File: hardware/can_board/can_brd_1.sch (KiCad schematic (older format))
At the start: 11 parts, among them P471 CONN_4, P472 CONN_2, U471 SN65HVD230

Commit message: making progress
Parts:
- added M470, M471: CONN_1, symbol CONN_1
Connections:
- no-connect marks 1 -> 3
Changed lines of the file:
@@
 Sheet 1 1
 Title ""
-Date "19 jan 2014"
+Date "26 jan 2014"
 Rev ""
 Comp ""
@@
 	2200 1550 2300 1550
 Wire Wire Line
-	4250 2150 3550 2150
-Wire Wire Line
-	4250 1550 3550 1550
+	4250 2150 4000 2150
+Wire Wire Line
+	4250 1550 4000 1550
 Text Label 5500 1750 0    60   ~ 0
 CANH
@@
 Wire Wire Line
 	5725 2625 5600 2625
-Text GLabel 3550 1550 0    60   Input ~ 0
-CAN_RX
-Text GLabel 3550 2150 0    60   Input ~ 0
-CAN_TX
+$Comp
+L CONN_1 M470
+U 1 1 52E4A990
+P 6600 1050
+F 0 "M470" H 6680 1050 40  0000 L CNN
+F 1 "CONN_1" H 6600 1105 30  0001 C CNN
+F 2 "" H 6600 1050 60  0000 C CNN
+F 3 "" H 6600 1050 60  0000 C CNN
+	1    6600 1050
+	1    0    0    -1
+$EndComp
+NoConn ~ 6450 1050
+$Comp
+L CONN_1 M471
+U 1 1 52E4A9A2
+P 6600 1200
+F 0 "M471" H 6680 1200 40  0000 L CNN
+F 1 "CONN_1" H 6600 1255 30  0001 C CNN
+F 2 "" H 6600 1200 60  0000 C CNN
+F 3 "" H 6600 1200 60  0000 C CNN
+	1    6600 1200
+	1    0    0    -1
+$EndComp
+NoConn ~ 6450 1200
 $EndSCHEMATC

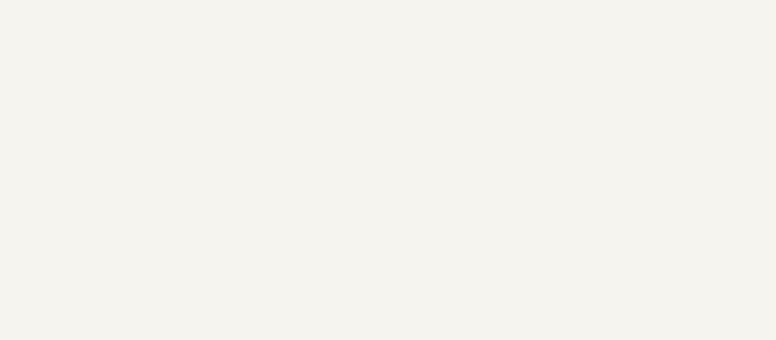
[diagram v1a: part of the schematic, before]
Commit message: 
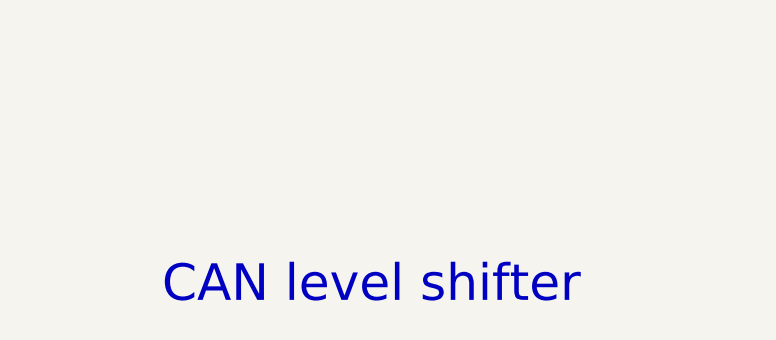
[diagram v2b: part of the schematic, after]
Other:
- note added: "CAN level shifter"
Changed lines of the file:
@@
 Sheet 1 1
 Title ""
-Date "26 jan 2014"
+Date "8 feb 2014"
 Rev ""
 Comp ""
@@
 $EndComp
 NoConn ~ 6450 1200
+Text Notes 5950 4200 0    160  ~ 0
+CAN level shifter
 $EndSCHEMATC

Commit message: 
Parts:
- added P1: CONN_2, symbol CONN_2
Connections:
- wire segments 16 -> 18
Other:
- note added: "pins"
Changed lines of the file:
@@
 LIBS:art-electro-ic
 LIBS:logo_flipped
-LIBS:can_brd_1-cache
-EELAYER 27 0
+EELAYER 24 0
 EELAYER END
 $Descr A4 11693 8268
@@
 Sheet 1 1
 Title ""
-Date "8 feb 2014"
+Date "16 Фев 2014"
 Rev ""
 Comp ""
@@
 Text Notes 5950 4200 0    160  ~ 0
 CAN level shifter
+$Comp
+L CONN_2 P1
+U 1 1 5300FF05
+P 7550 1850
+F 0 "P1" V 7500 1850 40  0000 C CNN
+F 1 "CONN_2" V 7600 1850 40  0000 C CNN
+F 2 "" H 7550 1850 60  0000 C CNN
+F 3 "" H 7550 1850 60  0000 C CNN
+	1    7550 1850
+	1    0    0    -1
+$EndComp
+Text Label 7100 1950 2    60   ~ 0
+CANH
+Text Label 7100 1750 2    60   ~ 0
+CANL
+Wire Wire Line
+	7200 1750 7100 1750
+Wire Wire Line
+	7200 1950 7100 1950
+Text Notes 6250 1600 0    60   ~ 0
+pins
 $EndSCHEMATC

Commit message: v 0.2 RC
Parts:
- removed D471: RED, symbol LED
- added D471: RED, symbol LED_0805
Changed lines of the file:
@@
 LIBS:power
 LIBS:device
-LIBS:transistors
 LIBS:conn
-LIBS:linear
-LIBS:regul
-LIBS:74xx
-LIBS:cmos4000
-LIBS:adc-dac
-LIBS:memory
-LIBS:xilinx
-LIBS:special
-LIBS:microcontrollers
-LIBS:dsp
-LIBS:microchip
-LIBS:analog_switches
-LIBS:motorola
-LIBS:texas
-LIBS:intel
-LIBS:audio
-LIBS:interface
-LIBS:digital-audio
-LIBS:philips
-LIBS:display
-LIBS:cypress
-LIBS:siliconi
-LIBS:opto
-LIBS:atmel
-LIBS:contrib
-LIBS:valves
+LIBS:logo_flipped
 LIBS:art-electro-ic
-LIBS:logo_flipped
+LIBS:art-electro-conn
+LIBS:can_brd_1-cache
 EELAYER 24 0
 EELAYER END
@@
 Sheet 1 1
 Title ""
-Date "16 Фев 2014"
+Date "20 Фев 2014"
 Rev ""
 Comp ""
@@
 $EndComp
 $Comp
-L LED D471
-U 1 1 52CAD8DC
-P 4350 3000
-F 0 "D471" H 4350 3100 50  0000 C CNN
-F 1 "RED" H 4350 2900 50  0000 C CNN
-F 2 "" H 4350 3000 60  0001 C CNN
-F 3 "" H 4350 3000 60  0001 C CNN
-	1    4350 3000
-	1    0    0    1
-$EndComp
-$Comp
 L GND #PWR01
 U 1 1 52CAD8DD
@@
 Text Notes 6250 1600 0    60   ~ 0
 pins
+$Comp
+L LED_0805 D471
+U 1 1 53060316
+P 4350 3000
+F 0 "D471" H 4350 3100 50  0000 C CNN
+F 1 "RED" H 4350 2900 50  0000 C CNN
+F 2 "" H 4350 3000 60  0000 C CNN
+F 3 "" H 4350 3000 60  0000 C CNN
+	1    4350 3000
+	1    0    0    -1
+$EndComp
 $EndSCHEMATC

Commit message: silkscreen improvements
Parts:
- removed M470: CONN_1, symbol CONN_1
- renumbered P1 to P473
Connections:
- no-connect marks 3 -> 2
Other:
- note added: "big pins"
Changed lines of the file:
@@
 Sheet 1 1
 Title ""
-Date "20 Фев 2014"
+Date "25 Фев 2014"
 Rev ""
 Comp ""
@@
 	5725 2625 5600 2625
 $Comp
-L CONN_1 M470
-U 1 1 52E4A990
-P 6600 1050
-F 0 "M470" H 6680 1050 40  0000 L CNN
-F 1 "CONN_1" H 6600 1105 30  0001 C CNN
-F 2 "" H 6600 1050 60  0000 C CNN
-F 3 "" H 6600 1050 60  0000 C CNN
-	1    6600 1050
-	1    0    0    -1
-$EndComp
-NoConn ~ 6450 1050
-$Comp
 L CONN_1 M471
 U 1 1 52E4A9A2
@@
 CAN level shifter
 $Comp
-L CONN_2 P1
+L CONN_2 P473
 U 1 1 5300FF05
 P 7550 1850
-F 0 "P1" V 7500 1850 40  0000 C CNN
+F 0 "P473" V 7500 1850 40  0000 C CNN
 F 1 "CONN_2" V 7600 1850 40  0000 C CNN
 F 2 "" H 7550 1850 60  0000 C CNN
@@
 	1    0    0    -1
 $EndComp
+Text Notes 7200 1600 0    60   ~ 0
+big pins
 $EndSCHEMATC
